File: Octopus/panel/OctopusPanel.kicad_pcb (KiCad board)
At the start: 2 copper layers, 211 x 38.4 mm, 43 parts, among them J1 To main board J11, SW1 228CMVARGBFDNR, SW2 228CMVARGBFDNR, SW3 228CMVARGBFDNR, SW4 228CMVARGBFDNR, SW5 228CMVARGBFDNR, SW6 228CMVARGBFDNR, SW7 228CMVARGBFDNR, SW8 228CMVARGBFDNR, U1 PCA9685PW, U2 PCA9685PW, U3 MCP23008-xSO

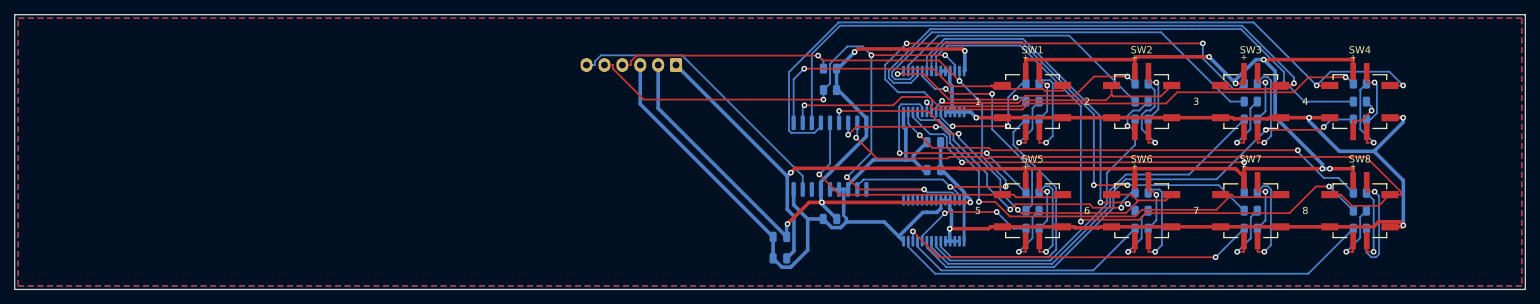
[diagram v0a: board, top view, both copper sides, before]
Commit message: Octopus: front-panel display + encoder, Omron B3W-9 buttons, DigiKey BOM
- Button board: 0.96" SSD1306 OLED (Winstar WEA012864D-03 on 5 mm
  spacers) and an Alps EC11E15204A3 encoder with push switch, left of
  the buttons. MCP23008 -> MCP23017 for the extra inputs (GPA7/GPB7
  unused: output-only on current silicon).
- Buttons: the discontinued CTS 228C RGB switches are replaced by Omron
  B3W-9000-RG2N (red + green LEDs): red = tip, green = ring, amber =
  both. One PCA9685 instead of two; LED resistors are four Bourns CAT16
  4-resistor arrays. Square 10.6 mm panel cut-outs.
- Firmware: Display (U8g2/U8x8, redraws only what changed), encoder
  decoding from the MCP23017 interrupt (half-cycle detents), SELECT? /
  push-to-load / 5 s timeout, presets shown and entered as 1-128,
  MidiHandler::recall(), bigger Serial1 RX buffer.
- Main board: status LEDs and their resistors removed (the buttons show
  every line); C2 value corrected to 22 uF 16 V.
- BOM_DigiKey.csv: full parts list by manufacturer part number
  (force-added: the repo ignores *.csv).
- ERC 0 errors on both boards; DRC 0 errors, 0 unconnected, 0 parity
  (main board: 16 vendor-footprint silkscreen-at-edge warnings).

Co-Authored-By: Claude Opus 5.5 <noreply@anthropic.com>
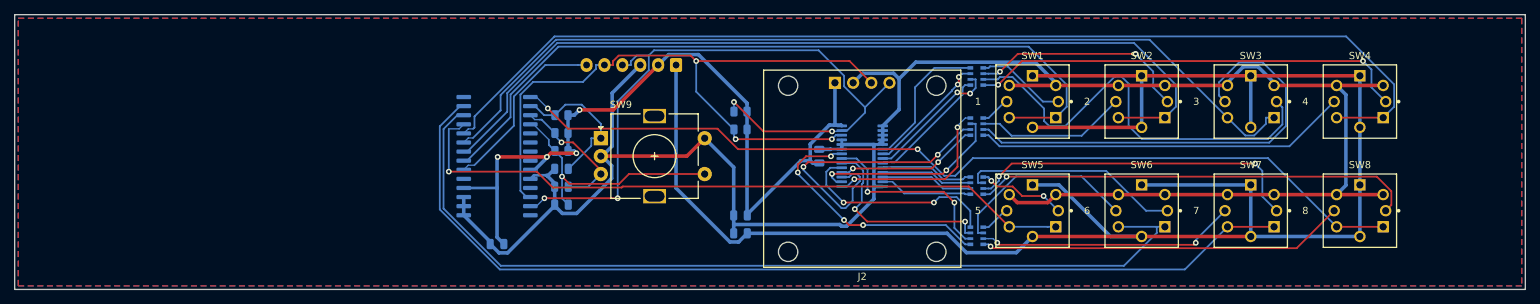
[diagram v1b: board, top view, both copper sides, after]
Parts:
- removed R10, R11, R13, R14, R16, R17, R19, R20, R22, R23, R7, R8: 390, Resistor_SMD:R_0805_2012Metric
- removed R12, R15, R18, R21, R24, R6, R9: 220, Resistor_SMD:R_0805_2012Metric
- removed R25, R26: 4.7k, Resistor_SMD:R_0805_2012Metric
- removed U2: PCA9685PW, Package_SO:TSSOP-28_4.4x9.7mm_P0.65mm
- added C6: 10n, Capacitor_SMD:C_0805_2012Metric, B.Cu at (119.0, 86.5)
- added C7: 10n, Capacitor_SMD:C_0805_2012Metric, B.Cu at (119.0, 89.0)
- added J2: WEA012864D-03 OLED, OctopusPanel:OLED_Winstar_WEA012864D-03, F.Cu at (161.0, 82.2)
- added RN1: 330, Resistor_SMD:R_Array_Convex_4x0603, B.Cu at (177.0, 71.1)
- added RN2: 330, Resistor_SMD:R_Array_Convex_4x0603, B.Cu at (177.0, 86.3)
- added RN3: 180, Resistor_SMD:R_Array_Convex_4x0603, B.Cu at (177.0, 78.1)
- added RN4: 180, Resistor_SMD:R_Array_Convex_4x0603, B.Cu at (177.0, 93.3)
- added SW9: EC11E15204A3, Rotary_Encoder:RotaryEncoder_Alps_EC11E-Switch_Vertical_H20mm, F.Cu at (124.5, 79.7)
- C3: value 100n -> 10u
- C5: value 10u -> 10n
- R1, R2: value 390 -> 4.7k
- R3: value 220 -> 10k
- R4, R5: value 390 -> 10k
- SW1, SW2, SW3, SW4, SW5, SW6, SW7, SW8: value 228CMVARGBFDNR -> B3W-9000-RG2N; footprint OctopusPanel:CTS_228CMV_RGB -> OctopusPanel:Omron_B3W-9_2LED_10x10
- U3: value MCP23008-xSO -> MCP23017; footprint Package_SO:SOIC-18W_7.5x11.6mm_P1.27mm -> Package_SO:SOIC-28W_7.5x17.9mm_P1.27mm
- moved R4 81.3 mm to (119.0, 79.0)
- moved R5 81.3 mm to (119.0, 81.5)
- moved R3 65.8 mm to (119.0, 76.5)
- moved C2 61.9 mm to (110.0, 94.5)
- moved U3 46.5 mm to (110.0, 82.2), turned to 180 degrees
- moved R1 41.0 mm to (144.0, 76.0)
- moved R2 41.0 mm to (144.0, 78.5)
- moved C5 33.0 mm to (119.0, 84.0)
- moved C1 16.1 mm to (155.0, 82.2), turned to 90 degrees
- moved U1 13.5 mm to (161.0, 82.2), turned to 180 degrees
- moved C3 12.5 mm to (144.0, 90.5)
- moved C4 5.52 mm to (144.0, 93.0)
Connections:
- C4 pad 1: +3V3 -> +5V
- C5 pad 1: +5V -> /ENC_A
- R1 pad 1: /LED1_R -> +3V3
- R1 pad 2: /DRV1_R -> /SDA
- R2 pad 1: /LED1_G -> +3V3
- R2 pad 2: /DRV1_G -> /SCL
- R3 pad 1: /LED1_B -> +3V3
- R3 pad 2: /DRV1_B -> /ENC_A
- R4 pad 1: /LED2_R -> +3V3
- R4 pad 2: /DRV2_R -> /ENC_B
- R5 pad 1: /LED2_G -> +3V3
- R5 pad 2: /DRV2_G -> /ENC_SW
- U3 pad 1: /SCL -> /BTN8
- U3 pad 10: /BTN1 -> GND
- U3 pad 11: /BTN2 -> unconnected-(U3-NC-Pad11)
- U3 pad 12: /BTN3 -> /SCL
- U3 pad 13: /BTN4 -> /SDA
- U3 pad 14: /BTN5 -> unconnected-(U3-NC-Pad14)
- U3 pad 15: /BTN6 -> GND
- U3 pad 16: /BTN7 -> GND
- U3 pad 17: /BTN8 -> GND
- U3 pad 2: /SDA -> /ENC_A
- U3 pad 3: GND -> /ENC_B
- U3 pad 4: GND -> /ENC_SW
- U3 pad 5: GND -> unconnected-(U3-GPB4-Pad5)
- U3 pad 6: +3V3 -> unconnected-(U3-GPB5-Pad6)
- U3 pad 8: /PANEL_INT -> unconnected-(U3-GPB7-Pad8)
- U3 pad 9: GND -> +3V3
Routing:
- net /DRV4_B: track 71.4 -> 0.00 mm, vias 2 -> 0
- net /DRV8_B: track 67.1 -> 0.00 mm
- net /BTN6: track 60.5 -> 126.9 mm, vias 3 -> 0
- net /BTN7: track 73.9 -> 138.6 mm, vias 3 -> 0
- net /BTN2: track 57.5 -> 121.4 mm, vias 1 -> 0
- net +5V: track 196.4 -> 256.8 mm, vias 6 -> 0
- net /DRV4_G: track 78.6 -> 20.1 mm, vias 0 -> 2
- net /BTN1: track 49.0 -> 106.6 mm, vias 1 -> 0
- net /DRV3_B: track 55.1 -> 0.00 mm
- net /LED3_G: track 9.42 -> 64.5 mm, vias 1 -> 0
- net /DRV8_R: track 67.9 -> 13.0 mm, vias 2 -> 0
- net /BTN5: track 43.3 -> 96.4 mm
- net /LED8_R: track 11.2 -> 62.0 mm
- net /DRV7_B: track 50.8 -> 0.00 mm, vias 2 -> 0
- net /LED4_R: track 11.9 -> 61.4 mm, vias 1 -> 2
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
